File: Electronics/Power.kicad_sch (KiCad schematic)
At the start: 0 parts

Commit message: Added third half bridge for BLDC applications
Signed-off-by: Finder <aki.kuusela@findersee.fi>
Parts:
- added C401, C402, C403, C404, C405, C406, C407, C408: C, Capacitor_SMD:C_0603_1608Metric_Pad1.08x0.95mm_HandSolder, symbol Device:C
- added H401, H402, H403, H404: MountingHole, MountingHole:MountingHole_3.2mm_M3, symbol Mechanical:MountingHole
- added U401: R-78B15-2.0, Converter_DCDC:Converter_DCDC_RECOM_R-78B-2.0_THT, symbol Regulator_Switching:R-78B15-2.0
- added U402: R-78E3.3-1.0, Converter_DCDC:Converter_DCDC_RECOM_R-78E-0.5_THT, symbol Regulator_Switching:R-78E3.3-1.0
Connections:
- new net +3V3: C407.1, C408.1, U402.3 (OUT)
- new net GND: C401.2, C402.2, C403.2, C404.2, C405.2, C406.2, C407.2, C408.2, U401.2 (GND), U402.2 (GND)
- new net VCC: C403.1, C404.1, C405.1, C406.1, U401.3 (OUT), U402.1 (IN)
- new net Vdrive: C401.1, C402.1, U401.1 (IN)

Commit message: Layout update
Signed-off-by: Aki Kuusela <git@findersee.fi>
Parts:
- removed U401: R-78B15-2.0, Converter_DCDC:Converter_DCDC_RECOM_R-78B-2.0_THT, symbol Regulator_Switching:R-78B15-2.0
- added U1: R-78C15-1.0, Converter_DCDC:Converter_DCDC_RECOM_R-78E-0.5_THT, symbol Regulator_Switching:R-78C15-1.0
- H401, H402, H403, H404: footprint MountingHole:MountingHole_3.2mm_M3 -> MountingHole:MountingHole_4mm
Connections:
- net GND: now also U1.2 (GND)
- net VCC: now also U1.3 (OUT)
- net Vdrive: now also U1.1 (IN)
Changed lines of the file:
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@@
       (effects (font (size 1.27 1.27)) (justify left) hide)
     )
-    (property "Footprint" "MountingHole:MountingHole_3.2mm_M3" (id 2) (at 162.56 172.72 0)
+    (property "Footprint" "MountingHole:MountingHole_4mm" (id 2) (at 162.56 172.72 0)
       (effects (font (size 1.27 1.27)) hide)
     )
@@
       (effects (font (size 1.27 1.27)) (justify left) hide)
     )
-    (property "Footprint" "MountingHole:MountingHole_3.2mm_M3" (id 2) (at 162.56 187.96 0)
+    (property "Footprint" "MountingHole:MountingHole_4mm" (id 2) (at 162.56 187.96 0)
       (effects (font (size 1.27 1.27)) hide)
     )
@@
     (pin "1")
     (pin "2")
+  )
+  (symbol (lib_id "Regulator_Switching:R-78C15-1.0") (at 125.73 53.34 0) (unit 1)
+    (in_bom yes) (on_board yes) (fields_autoplaced)
+    (property "Reference" "U1" (id 0) (at 125.73 45.72 0))
+    (property "Value" "R-78C15-1.0" (id 1) (at 125.73 48.26 0))
+    (property "Footprint" "Converter_DCDC:Converter_DCDC_RECOM_R-78E-0.5_THT" (id 2) (at 127 59.69 0)
+      (effects (font (size 1.27 1.27) italic) (justify left) hide)
+    )
+    (property "Datasheet" "https://www.recom-power.com/pdf/Innoline/R-78Cxx-1.0.pdf" (id 3) (at 125.73 53.34 0)
+      (effects (font (size 1.27 1.27)) hide)
+    )
+    (pin "1")
+    (pin "2")
+    (pin "3")
   )
   (symbol (lib_id "power:+3V3") (at 259.08 50.8 0) (unit 1)
@@
       (effects (font (size 1.27 1.27)) (justify left) hide)
     )
-    (property "Footprint" "MountingHole:MountingHole_3.2mm_M3" (id 2) (at 162.56 177.8 0)
+    (property "Footprint" "MountingHole:MountingHole_4mm" (id 2) (at 162.56 177.8 0)
       (effects (font (size 1.27 1.27)) hide)
     )
@@
       (effects (font (size 1.27 1.27)) (justify left) hide)
     )
-    (property "Footprint" "MountingHole:MountingHole_3.2mm_M3" (id 2) (at 162.56 182.88 0)
+    (property "Footprint" "MountingHole:MountingHole_4mm" (id 2) (at 162.56 182.88 0)
       (effects (font (size 1.27 1.27)) hide)
     )
@@
     (pin "2")
   )
-  (symbol (lib_id "Regulator_Switching:R-78B15-2.0") (at 125.73 53.34 0) (unit 1)
-    (in_bom yes) (on_board yes) (fields_autoplaced)
-    (property "Reference" "U401" (id 0) (at 125.73 47.4685 0))
-    (property "Value" "R-78B15-2.0" (id 1) (at 125.73 50.2436 0))
-    (property "Footprint" "Converter_DCDC:Converter_DCDC_RECOM_R-78B-2.0_THT" (id 2) (at 127 59.69 0)
-      (effects (font (size 1.27 1.27) italic) (justify left) hide)
-    )
-    (property "Datasheet" "https://www.recom-power.com/pdf/Innoline/R-78Bxx-2.0.pdf" (id 3) (at 125.73 53.34 0)
-      (effects (font (size 1.27 1.27)) hide)
-    )
-    (pin "1")
-    (pin "2")
-    (pin "3")
-  )
   (symbol (lib_id "power:GND") (at 125.73 71.12 0) (unit 1)

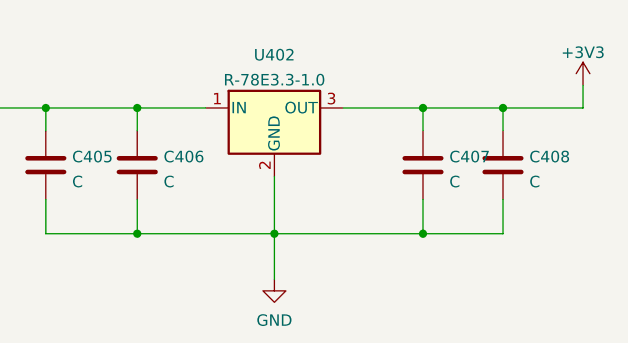
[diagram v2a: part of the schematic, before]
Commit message: Added hall sensor circuitry
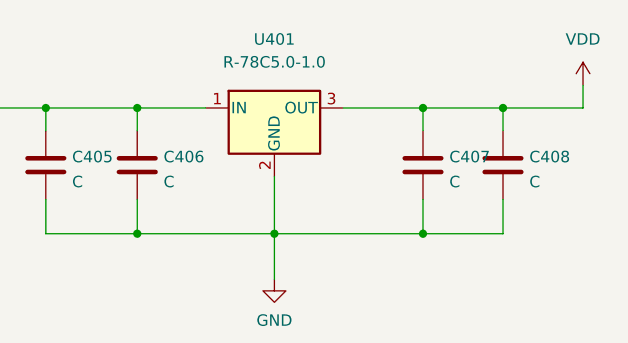
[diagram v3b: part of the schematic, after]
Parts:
- removed U402: R-78E3.3-1.0, Converter_DCDC:Converter_DCDC_RECOM_R-78E-0.5_THT, symbol Regulator_Switching:R-78E3.3-1.0
- added U401: R-78C5.0-1.0, Converter_DCDC:Converter_DCDC_RECOM_R-78E-0.5_THT, symbol Regulator_Switching:R-78C5.0-1.0
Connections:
- net GND: now also U401.2 (GND)
- net VCC: now also U401.1 (IN)
- net +3V3 renamed VDD
- net VDD: now also U401.3 (OUT)

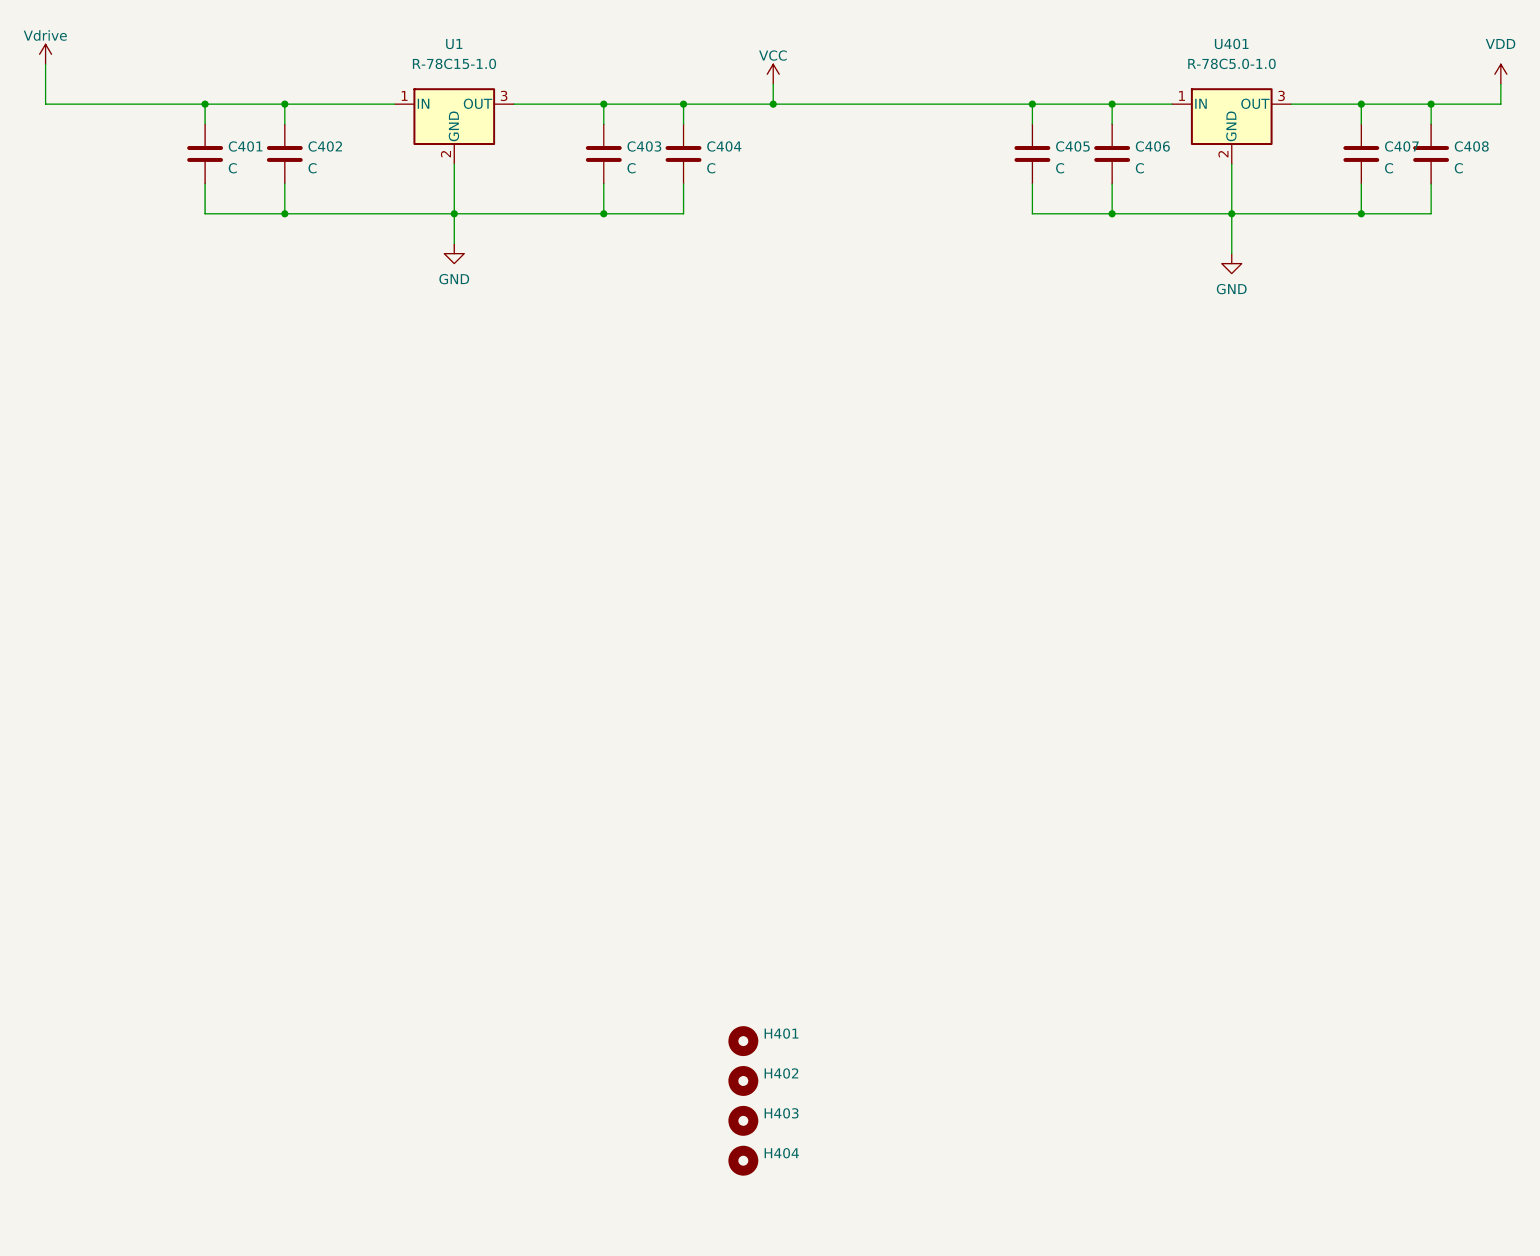
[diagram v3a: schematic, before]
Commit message: Added current sensor circuitry
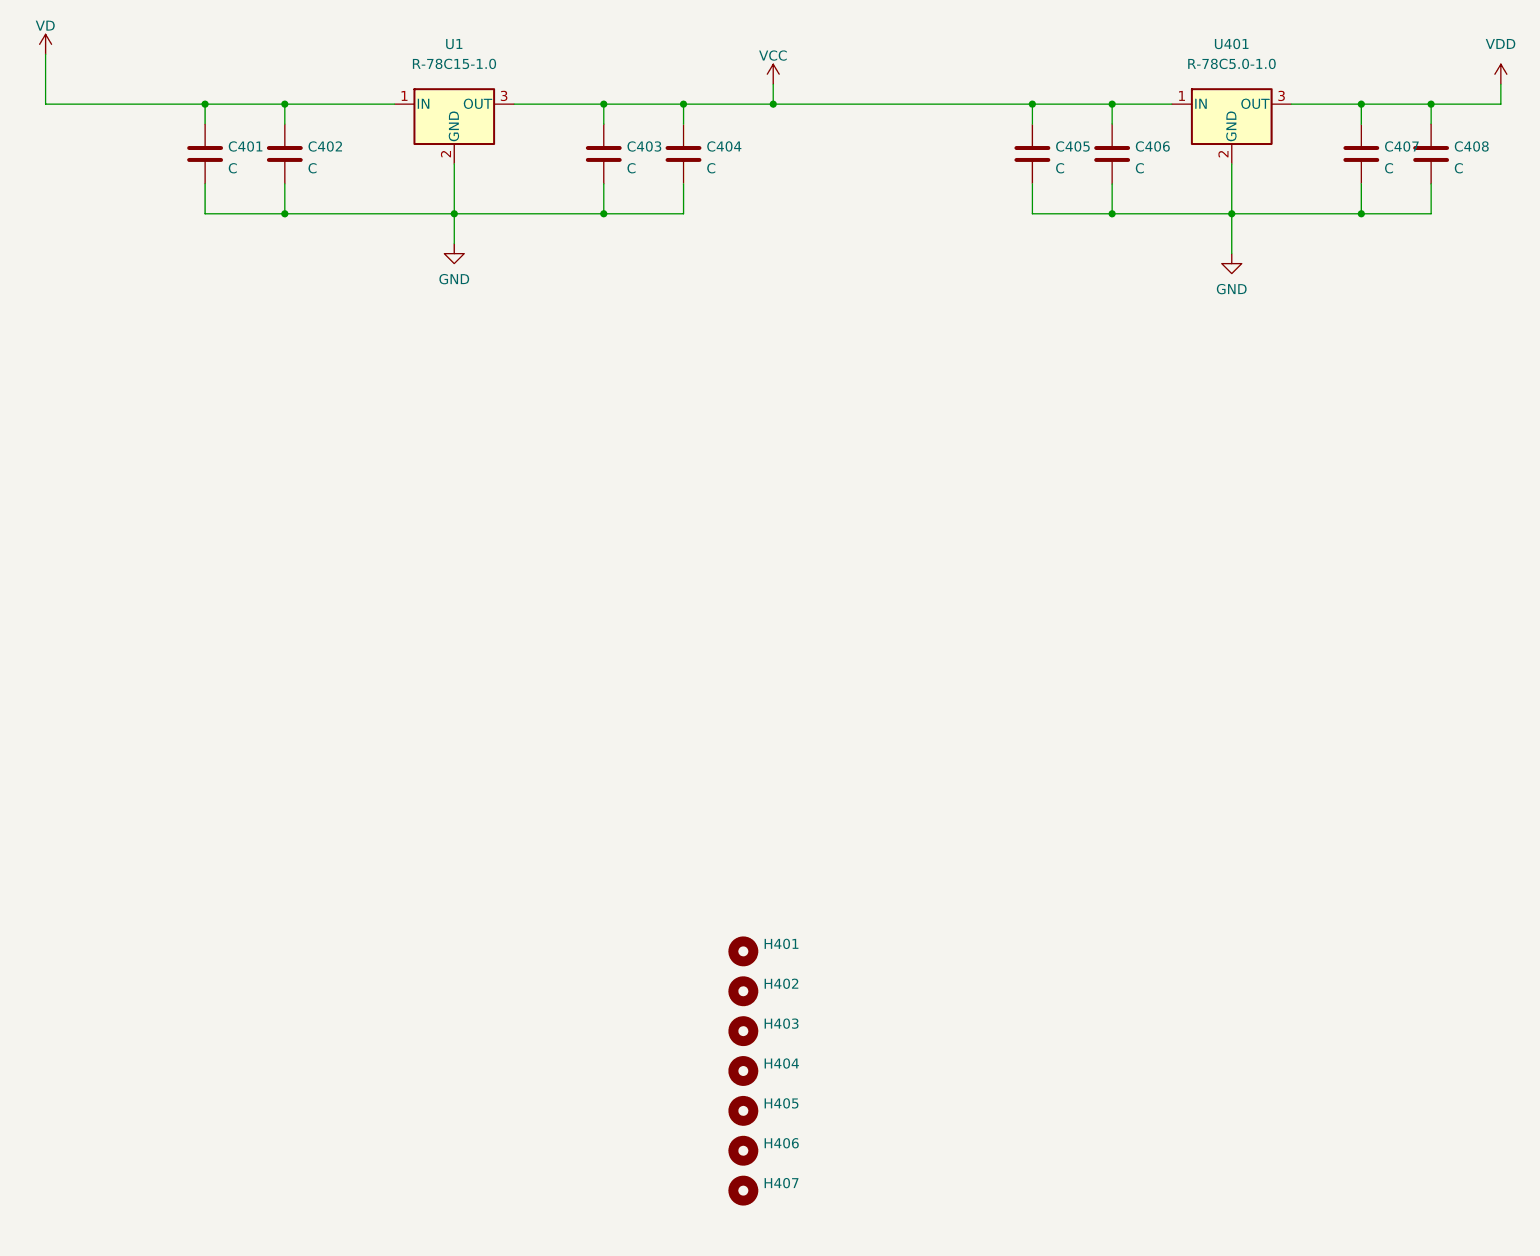
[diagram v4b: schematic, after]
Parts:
- added H405, H406, H407: MountingHole, MountingHole:MountingHole_3.2mm_M3_DIN965, symbol Mechanical:MountingHole
- H401, H402, H403, H404: footprint MountingHole:MountingHole_4mm -> MountingHole:MountingHole_3.2mm_M3_DIN965
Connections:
- net Vdrive renamed VD
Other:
- moved on the sheet: H401, H402, H403, H404
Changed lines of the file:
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@@
     (stroke (width 0) (type default) (color 0 0 0 0))
   )
-  (wire (pts (xy 73.66 48.26) (xy 73.66 53.34))
+  (wire (pts (xy 73.66 46.99) (xy 73.66 53.34))
     (stroke (width 0) (type default) (color 0 0 0 0))
   )
@@
     (pin "3")
   )
-  (symbol (lib_name "MountingHole_1") (lib_id "Mechanical:MountingHole") (at 162.56 172.72 0) (unit 1)
-    (in_bom yes) (on_board yes) (fields_autoplaced)
-    (property "Reference" "H401" (id 0) (at 165.1 171.8115 0)
-      (effects (font (size 1.27 1.27)) (justify left))
-    )
-    (property "Value" "MountingHole" (id 1) (at 165.1 174.5866 0)
-      (effects (font (size 1.27 1.27)) (justify left) hide)
-    )
-    (property "Footprint" "MountingHole:MountingHole_4mm" (id 2) (at 162.56 172.72 0)
-      (effects (font (size 1.27 1.27)) hide)
-    )
-    (property "Datasheet" "~" (id 3) (at 162.56 172.72 0)
-      (effects (font (size 1.27 1.27)) hide)
-    )
-  )
-  (symbol (lib_name "MountingHole_1") (lib_id "Mechanical:MountingHole") (at 162.56 187.96 0) (unit 1)
-    (in_bom yes) (on_board yes) (fields_autoplaced)
-    (property "Reference" "H404" (id 0) (at 165.1 187.0515 0)
-      (effects (font (size 1.27 1.27)) (justify left))
-    )
-    (property "Value" "MountingHole" (id 1) (at 165.1 189.8266 0)
-      (effects (font (size 1.27 1.27)) (justify left) hide)
-    )
-    (property "Footprint" "MountingHole:MountingHole_4mm" (id 2) (at 162.56 187.96 0)
-      (effects (font (size 1.27 1.27)) hide)
-    )
-    (property "Datasheet" "~" (id 3) (at 162.56 187.96 0)
+  (symbol (lib_name "MountingHole_1") (lib_id "Mechanical:MountingHole") (at 162.56 161.29 0) (unit 1)
+    (in_bom yes) (on_board yes) (fields_autoplaced)
+    (property "Reference" "H401" (id 0) (at 165.1 160.3815 0)
+      (effects (font (size 1.27 1.27)) (justify left))
+    )
+    (property "Value" "MountingHole" (id 1) (at 165.1 163.1566 0)
+      (effects (font (size 1.27 1.27)) (justify left) hide)
+    )
+    (property "Footprint" "MountingHole:MountingHole_3.2mm_M3_DIN965" (id 2) (at 162.56 161.29 0)
+      (effects (font (size 1.27 1.27)) hide)
+    )
+    (property "Datasheet" "~" (id 3) (at 162.56 161.29 0)
+      (effects (font (size 1.27 1.27)) hide)
+    )
+  )
+  (symbol (lib_name "MountingHole_1") (lib_id "Mechanical:MountingHole") (at 162.56 176.53 0) (unit 1)
+    (in_bom yes) (on_board yes) (fields_autoplaced)
+    (property "Reference" "H404" (id 0) (at 165.1 175.6215 0)
+      (effects (font (size 1.27 1.27)) (justify left))
+    )
+    (property "Value" "MountingHole" (id 1) (at 165.1 178.3966 0)
+      (effects (font (size 1.27 1.27)) (justify left) hide)
+    )
+    (property "Footprint" "MountingHole:MountingHole_3.2mm_M3_DIN965" (id 2) (at 162.56 176.53 0)
+      (effects (font (size 1.27 1.27)) hide)
+    )
+    (property "Datasheet" "~" (id 3) (at 162.56 176.53 0)
       (effects (font (size 1.27 1.27)) hide)
     )
@@
     (pin "2")
   )
-  (symbol (lib_name "MountingHole_1") (lib_id "Mechanical:MountingHole") (at 162.56 177.8 0) (unit 1)
-    (in_bom yes) (on_board yes) (fields_autoplaced)
-    (property "Reference" "H402" (id 0) (at 165.1 176.8915 0)
-      (effects (font (size 1.27 1.27)) (justify left))
-    )
-    (property "Value" "MountingHole" (id 1) (at 165.1 179.6666 0)
-      (effects (font (size 1.27 1.27)) (justify left) hide)
-    )
-    (property "Footprint" "MountingHole:MountingHole_4mm" (id 2) (at 162.56 177.8 0)
-      (effects (font (size 1.27 1.27)) hide)
-    )
-    (property "Datasheet" "~" (id 3) (at 162.56 177.8 0)
+  (symbol (lib_name "MountingHole_1") (lib_id "Mechanical:MountingHole") (at 162.56 166.37 0) (unit 1)
+    (in_bom yes) (on_board yes) (fields_autoplaced)
+    (property "Reference" "H402" (id 0) (at 165.1 165.4615 0)
+      (effects (font (size 1.27 1.27)) (justify left))
+    )
+    (property "Value" "MountingHole" (id 1) (at 165.1 168.2366 0)
+      (effects (font (size 1.27 1.27)) (justify left) hide)
+    )
+    (property "Footprint" "MountingHole:MountingHole_3.2mm_M3_DIN965" (id 2) (at 162.56 166.37 0)
+      (effects (font (size 1.27 1.27)) hide)
+    )
+    (property "Datasheet" "~" (id 3) (at 162.56 166.37 0)
       (effects (font (size 1.27 1.27)) hide)
     )
@@
     (pin "2")
   )
-  (symbol (lib_name "MountingHole_1") (lib_id "Mechanical:MountingHole") (at 162.56 182.88 0) (unit 1)
-    (in_bom yes) (on_board yes) (fields_autoplaced)
-    (property "Reference" "H403" (id 0) (at 165.1 181.9715 0)
-      (effects (font (size 1.27 1.27)) (justify left))
-    )
-    (property "Value" "MountingHole" (id 1) (at 165.1 184.7466 0)
-      (effects (font (size 1.27 1.27)) (justify left) hide)
-    )
-    (property "Footprint" "MountingHole:MountingHole_4mm" (id 2) (at 162.56 182.88 0)
-      (effects (font (size 1.27 1.27)) hide)
-    )
-    (property "Datasheet" "~" (id 3) (at 162.56 182.88 0)
+  (symbol (lib_name "MountingHole_1") (lib_id "Mechanical:MountingHole") (at 162.56 171.45 0) (unit 1)
+    (in_bom yes) (on_board yes) (fields_autoplaced)
+    (property "Reference" "H403" (id 0) (at 165.1 170.5415 0)
+      (effects (font (size 1.27 1.27)) (justify left))
+    )
+    (property "Value" "MountingHole" (id 1) (at 165.1 173.3166 0)
+      (effects (font (size 1.27 1.27)) (justify left) hide)
+    )
+    (property "Footprint" "MountingHole:MountingHole_3.2mm_M3_DIN965" (id 2) (at 162.56 171.45 0)
+      (effects (font (size 1.27 1.27)) hide)
+    )
+    (property "Datasheet" "~" (id 3) (at 162.56 171.45 0)
+      (effects (font (size 1.27 1.27)) hide)
+    )
+  )
+  (symbol (lib_name "MountingHole_1") (lib_id "Mechanical:MountingHole") (at 162.56 186.69 0) (unit 1)
+    (in_bom yes) (on_board yes) (fields_autoplaced)
+    (property "Reference" "H406" (id 0) (at 165.1 185.7815 0)
+      (effects (font (size 1.27 1.27)) (justify left))
+    )
+    (property "Value" "MountingHole" (id 1) (at 165.1 188.5566 0)
+      (effects (font (size 1.27 1.27)) (justify left) hide)
+    )
+    (property "Footprint" "MountingHole:MountingHole_3.2mm_M3_DIN965" (id 2) (at 162.56 186.69 0)
+      (effects (font (size 1.27 1.27)) hide)
+    )
+    (property "Datasheet" "~" (id 3) (at 162.56 186.69 0)
       (effects (font (size 1.27 1.27)) hide)
     )
@@
     (pin "2")
   )
-  (symbol (lib_id "power:Vdrive") (at 73.66 48.26 0) (unit 1)
-    (in_bom yes) (on_board yes) (fields_autoplaced)
-    (property "Reference" "#PWR0119" (id 0) (at 68.58 52.07 0)
-      (effects (font (size 1.27 1.27)) hide)
-    )
-    (property "Value" "Vdrive" (id 1) (at 73.66 44.6555 0))
-    (property "Footprint" "" (id 2) (at 73.66 48.26 0)
-      (effects (font (size 1.27 1.27)) hide)
-    )
-    (property "Datasheet" "" (id 3) (at 73.66 48.26 0)
+  (symbol (lib_id "power:VD") (at 73.66 46.99 0) (unit 1)
+    (in_bom yes) (on_board yes) (fields_autoplaced)
+    (property "Reference" "#PWR0119" (id 0) (at 73.66 50.8 0)
+      (effects (font (size 1.27 1.27)) hide)
+    )
+    (property "Value" "VD" (id 1) (at 73.66 43.3855 0))
+    (property "Footprint" "" (id 2) (at 73.66 46.99 0)
+      (effects (font (size 1.27 1.27)) hide)
+    )
+    (property "Datasheet" "" (id 3) (at 73.66 46.99 0)
       (effects (font (size 1.27 1.27)) hide)
     )
@@
     (pin "2")
   )
+  (symbol (lib_name "MountingHole_1") (lib_id "Mechanical:MountingHole") (at 162.56 181.61 0) (unit 1)
+    (in_bom yes) (on_board yes) (fields_autoplaced)
+    (property "Reference" "H405" (id 0) (at 165.1 180.7015 0)
+      (effects (font (size 1.27 1.27)) (justify left))
+    )
+    (property "Value" "MountingHole" (id 1) (at 165.1 183.4766 0)
+      (effects (font (size 1.27 1.27)) (justify left) hide)
+    )
+    (property "Footprint" "MountingHole:MountingHole_3.2mm_M3_DIN965" (id 2) (at 162.56 181.61 0)
+      (effects (font (size 1.27 1.27)) hide)
+    )
+    (property "Datasheet" "~" (id 3) (at 162.56 181.61 0)
+      (effects (font (size 1.27 1.27)) hide)
+    )
+  )
+  (symbol (lib_name "MountingHole_1") (lib_id "Mechanical:MountingHole") (at 162.56 191.77 0) (unit 1)
+    (in_bom yes) (on_board yes) (fields_autoplaced)
+    (property "Reference" "H407" (id 0) (at 165.1 190.8615 0)
+      (effects (font (size 1.27 1.27)) (justify left))
+    )
+    (property "Value" "MountingHole" (id 1) (at 165.1 193.6366 0)
+      (effects (font (size 1.27 1.27)) (justify left) hide)
+    )
+    (property "Footprint" "MountingHole:MountingHole_3.2mm_M3_DIN965" (id 2) (at 162.56 191.77 0)
+      (effects (font (size 1.27 1.27)) hide)
+    )
+    (property "Datasheet" "~" (id 3) (at 162.56 191.77 0)
+      (effects (font (size 1.27 1.27)) hide)
+    )
+  )
   (symbol (lib_id "power:GND") (at 125.73 71.12 0) (unit 1)
